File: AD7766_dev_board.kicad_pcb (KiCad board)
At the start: 2 copper layers, 80 x 63.5 mm, 62 parts, among them J1 Conn_Coaxial, J2 Conn_Coaxial, J3 Conn_01x06_Male, J4 Conn_01x10_Male, U1 PWR_JACK_POS, U2 PWR_JACK_GND, U3 ADR445, U4 ADP3330-5, U5 ADP3330-2.5, U6 ADP3330-2.5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

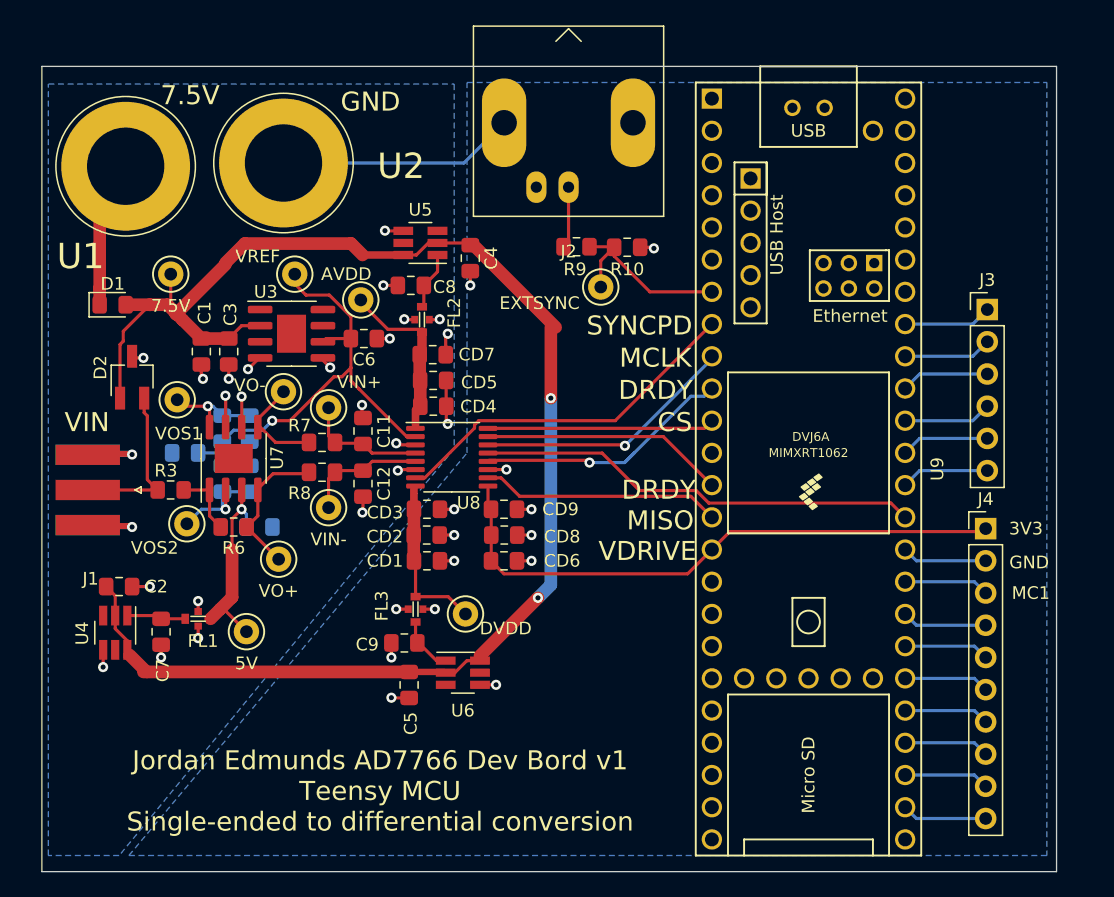
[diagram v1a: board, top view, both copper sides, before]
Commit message: updated with errors found in version 1, sending out version 2 for fabrication
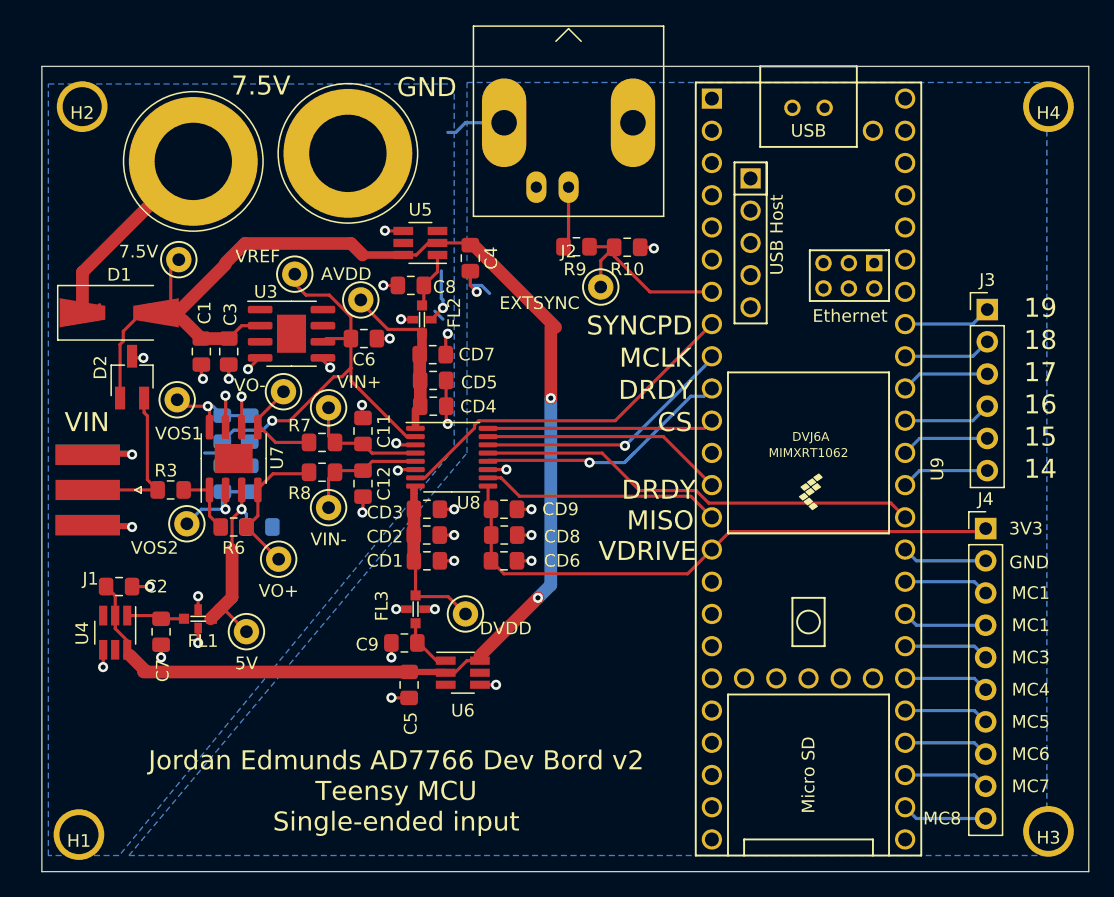
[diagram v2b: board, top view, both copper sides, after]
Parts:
- removed C13: 10uF, Capacitor_SMD:C_0805_2012Metric_Pad1.15x1.40mm_HandSolder
- added H1: MountingHole, my_library_foot:m3_mounting_hole, F.Cu at (-17.4, 28.8)
- added H2: MountingHole, my_library_foot:m3_mounting_hole, F.Cu at (-17.1, -28.6)
- added H3: MountingHole, my_library_foot:m3_mounting_hole, F.Cu at (59.1, 28.6)
- added H4: MountingHole, my_library_foot:m3_mounting_hole, F.Cu at (59.1, -28.6)
- D1: footprint Diode_SMD:D_0805_2012Metric_Pad1.15x1.40mm_HandSolder -> Diode_SMD:D_SMA-SMB_Universal_Handsoldering
- R1: value 1k -> 3k
- R2: value 3k -> 1k
- moved U1 5.35 mm to (-8.38, -24.3)
- moved U2 5.14 mm to (3.81, -24.9)
- moved TP1 1.31 mm to (-9.53, -16.5)
- moved D1 0.82 mm to (-14.2, -12.3)
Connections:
- U3 pad 5: GND -> Net-(U3-Pad5)
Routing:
- net GND: track 82.9 -> 74.9 mm, vias 39 -> 38
- net Net-(D1-Pad1): track 11.6 -> 17.2 mm
- net +7.5V: track 122.1 -> 120.8 mm
- net Net-(U3-Pad5): track 0.00 -> 1.00 mm, vias 0 -> 1
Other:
- board size 80 x 63.5 mm -> 82.5 x 63.5 mm
- board text added: "14"
- board text added: "15"
- board text added: "16"
- board text added: "17"
- board text added: "18"
- board text added: "19"
- board text added: "Jordan Edmunds AD7766 Dev Bord v2 Teensy MCU Single-ended input"
- board text added: "MC3"
- board text added: "MC4"
- board text added: "MC5"
- board text added: "MC6"
- board text added: "MC7"
- board text added: "MC8"
- board text removed: "Jordan Edmunds AD7766 Dev Bord v1 Teensy MCU Single-ended to differential conversion"

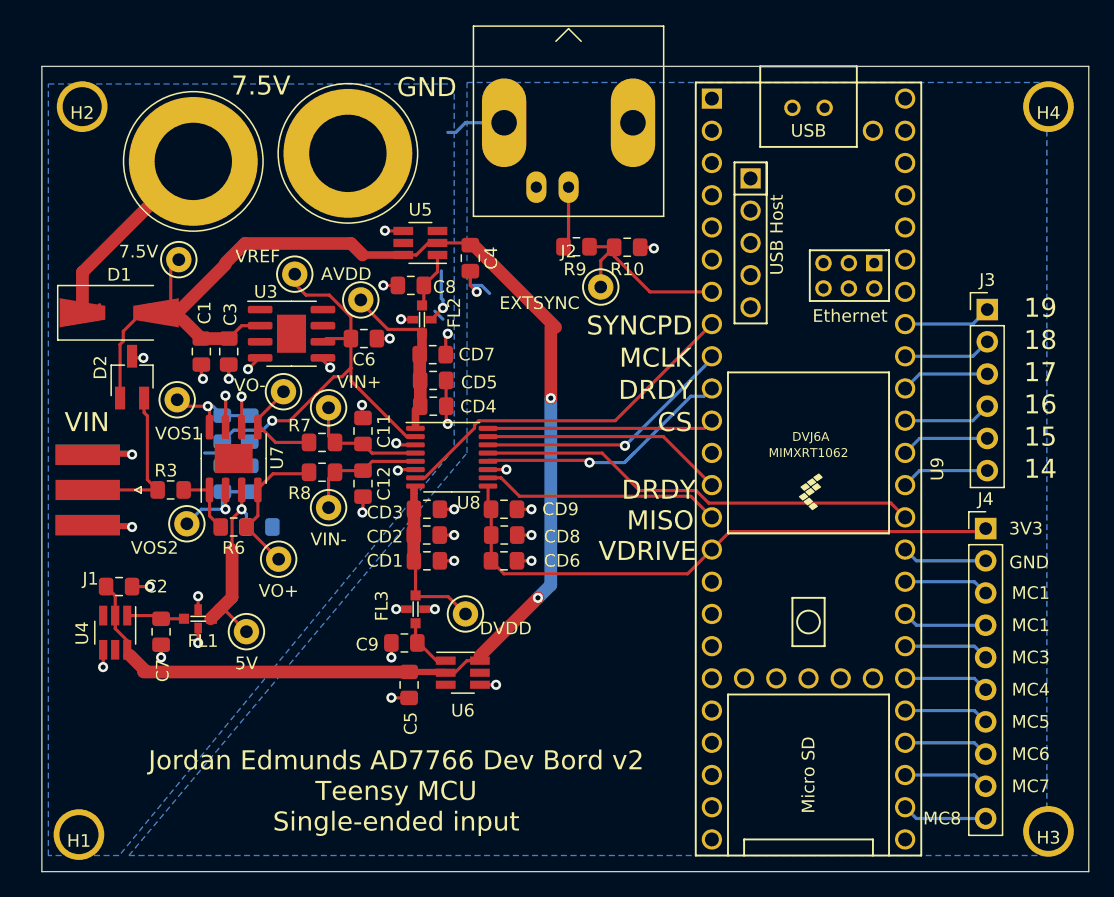
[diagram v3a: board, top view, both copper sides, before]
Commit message: found issue of MCLK not being divided down to 2.5V, but remaining at 3.3V. Fixed issue on PCB, added to README
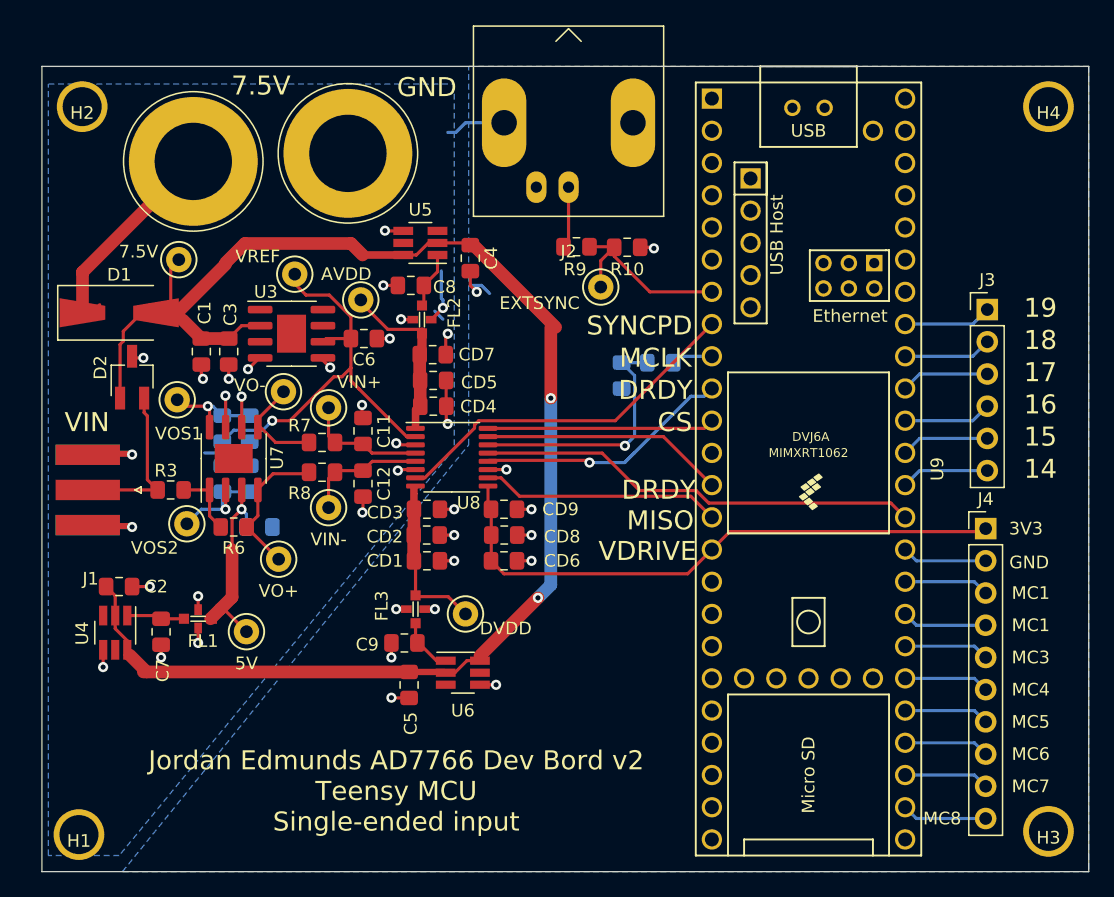
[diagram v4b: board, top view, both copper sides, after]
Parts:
- added R11: 1k, Resistor_SMD:R_0805_2012Metric_Pad1.15x1.40mm_HandSolder, B.Cu at (25.4, -7.37)
- added R12: 320, Resistor_SMD:R_0805_2012Metric_Pad1.15x1.40mm_HandSolder, B.Cu at (28.4, -8.38)
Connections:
- U9 pad 9: /MCLK -> Net-(R12-Pad1)
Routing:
- net Net-(R12-Pad1): track 0.00 -> 3.46 mm
- net /MCLK: track 20.7 -> 20.2 mm

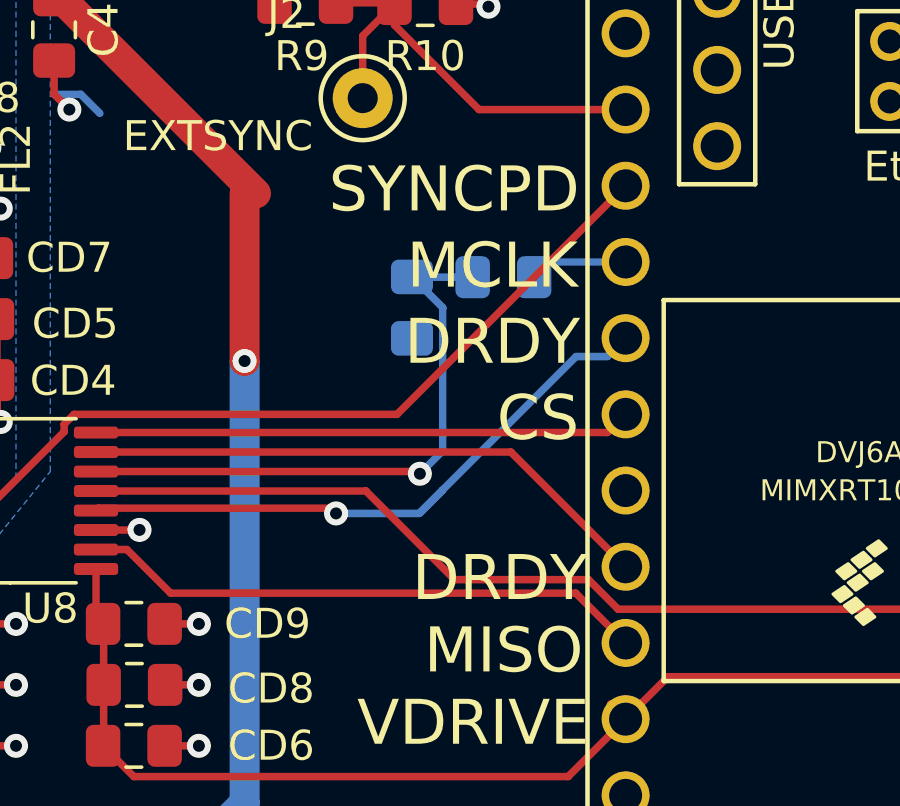
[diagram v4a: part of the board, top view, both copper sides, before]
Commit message: updated PCB to add voltage divider to SYNC/PD pin
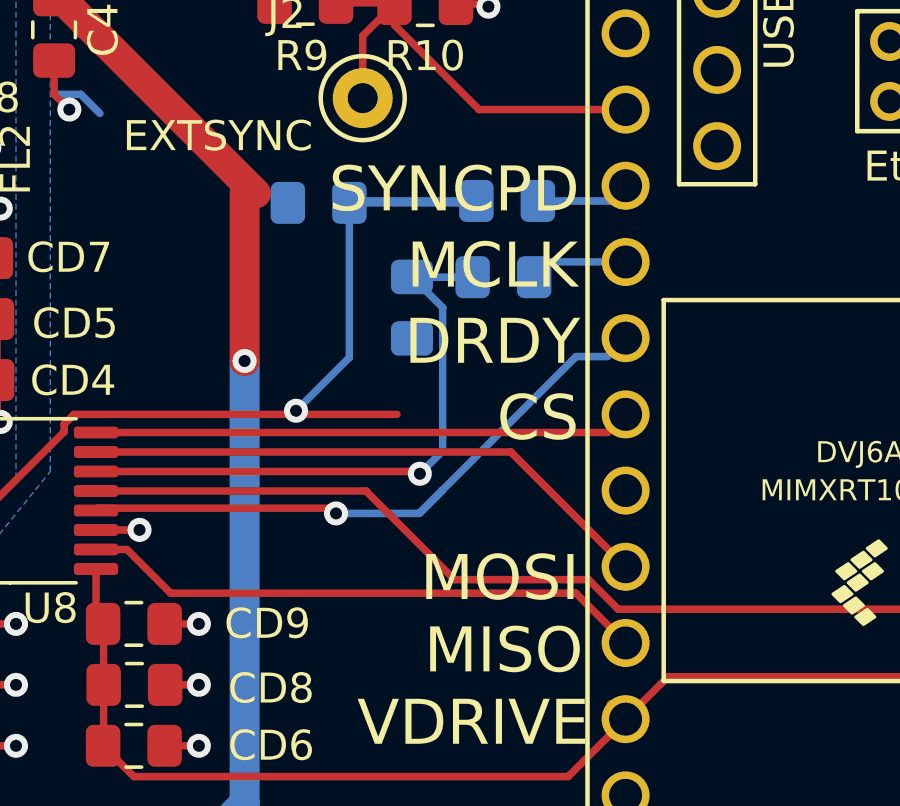
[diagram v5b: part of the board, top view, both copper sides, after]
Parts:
- added R13: 1k, Resistor_SMD:R_0805_2012Metric_Pad1.15x1.40mm_HandSolder, B.Cu at (22.3, -10.9)
- added R14: 320R, Resistor_SMD:R_0805_2012Metric_Pad1.15x1.40mm_HandSolder, B.Cu at (28.6, -10.9)
- C6: value 100nF -> 10uF
- R1: value 3k -> 30k
- R2, R4, R5: value 1k -> 10k
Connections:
- U9 pad 8: /SYNCPD -> Net-(R14-Pad1)
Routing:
- net /SYNCPD: track 28.5 -> 34.2 mm, vias 0 -> 1
- net Net-(R14-Pad1): track 0.00 -> 3.13 mm
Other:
- board text added: "MOSI"
